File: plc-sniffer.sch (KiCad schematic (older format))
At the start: 3 parts, among them J101 TO EVSE, J102 DEBUG, J103 TO EV

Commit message: Add files via upload
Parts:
- J101, J102, J103: footprint (none) -> Connector_PinHeader_2.54mm:PinHeader_1x03_P2.54mm_Vertical
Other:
- note added: "0,1"
- note added: "2020/06/19"
- note added: "PLC Sniffer"
- note added: "Top layer schematic for\nPLC man-in-the-middle sniffer\nwith 15118 charging interface"
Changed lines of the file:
@@
 F 0 "J101" H 2418 3125 50  0000 C CNN
 F 1 "TO EVSE" H 2418 3216 50  0000 C CNN
-F 2 "" H 2500 3450 50  0001 C CNN
+F 2 "Connector_PinHeader_2.54mm:PinHeader_1x03_P2.54mm_Vertical" H 2500 3450 50  0001 C CNN
 F 3 "~" H 2500 3450 50  0001 C CNN
 	1    2500 3450
@@
 F 0 "J103" H 8830 3542 50  0000 L CNN
 F 1 "TO EV" H 8830 3451 50  0000 L CNN
-F 2 "" H 8750 3500 50  0001 C CNN
+F 2 "Connector_PinHeader_2.54mm:PinHeader_1x03_P2.54mm_Vertical" H 8750 3500 50  0001 C CNN
 F 3 "~" H 8750 3500 50  0001 C CNN
 	1    8750 3500
@@
 F 0 "J102" H 6980 2842 50  0000 L CNN
 F 1 "DEBUG" H 6980 2751 50  0000 L CNN
-F 2 "" H 6900 2800 50  0001 C CNN
+F 2 "Connector_PinHeader_2.54mm:PinHeader_1x03_P2.54mm_Vertical" H 6900 2800 50  0001 C CNN
 F 3 "~" H 6900 2800 50  0001 C CNN
 	1    6900 2800
@@
 Wire Wire Line
 	6450 5150 6900 5150
+Text Notes 7350 7500 0    50   ~ 0
+PLC Sniffer
+Text Notes 10600 7650 0    50   ~ 0
+0,1
+Text Notes 8100 7650 0    50   ~ 0
+2020/06/19
+Text Notes 7050 7050 0    100  ~ 0
+Top layer schematic for\nPLC man-in-the-middle sniffer\nwith 15118 charging interface
 $EndSCHEMATC

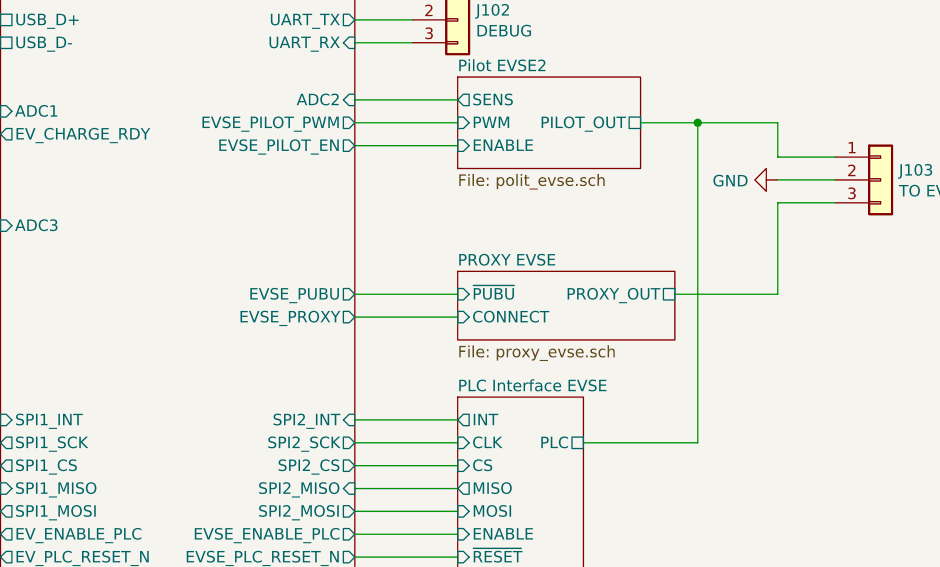
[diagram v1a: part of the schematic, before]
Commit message: Submited for production & smt assembly
v0.01
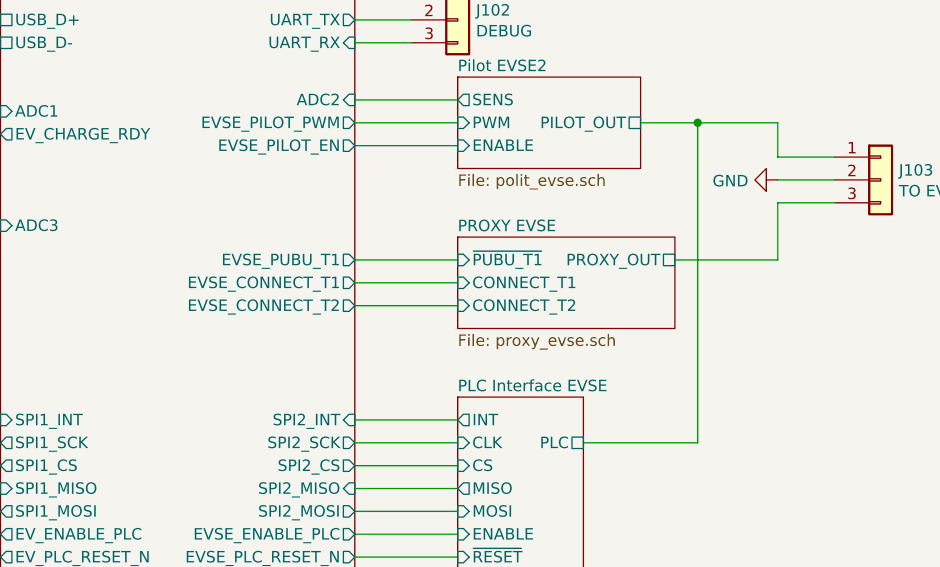
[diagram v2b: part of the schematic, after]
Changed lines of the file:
@@
-$EndSheet
-$Sheet
-S 6900 3900 950  300
-U 5EF016C6
-F0 "PROXY EVSE" 50
-F1 "proxy_evse.sch" 50
-F2 "PROXY_OUT" U R 7850 4000 50
-F3 "CONNECT" I L 6900 4100 50
-F4 "~PUBU" I L 6900 4000 50
 $EndSheet
 $Sheet
@@
 F5 "USB_D+" U L 4900 2800 50
 F6 "EVSE_PILOT_PWM" O R 6450 3250 50
-F7 "EVSE_PROXY" O R 6450 4100 50
-F8 "EVSE_PUBU" O R 6450 4000 50
-F9 "ADC1" I L 4900 3200 50
-F10 "ETH_CLK" I L 4900 6450 50
-F11 "ETH_MDIO" U L 4900 6250 50
-F12 "SPI1_SCK" O L 4900 4650 50
-F13 "SPI1_MISO" I L 4900 4850 50
-F14 "ETH_CRS_DV" I L 4900 5550 50
-F15 "SPI1_MOSI" O L 4900 4950 50
-F16 "ETH_TX_EN" O L 4900 5850 50
-F17 "ETH_TXD0" O L 4900 6050 50
-F18 "ETH_TXD1" O L 4900 5950 50
-F19 "ETH_MDC" O L 4900 6150 50
-F20 "ETH_RXD0" I L 4900 5750 50
-F21 "ETH_RXD1" I L 4900 5650 50
-F22 "MCO_2" O L 4900 6350 50
-F23 "SPI1_CS" O L 4900 4750 50
-F24 "SPI2_SCK" O R 6450 4650 50
-F25 "SPI2_MISO" I R 6450 4850 50
-F26 "SPI2_MOSI" O R 6450 4950 50
-F27 "SPI2_CS" O R 6450 4750 50
-F28 "EV_CHARGE_RDY" O L 4900 3300 50
-F29 "SPI2_INT" I R 6450 4550 50
-F30 "SPI1_INT" I L 4900 4550 50
-F31 "EV_ENABLE_PLC" O L 4900 5050 50
-F32 "EVSE_ENABLE_PLC" O R 6450 5050 50
-F33 "EVSE_PILOT_EN" O R 6450 3350 50
-F34 "~PHY_RESET" O L 4900 6750 50
-F35 "PHY_PDOWN" O L 4900 6850 50
-F36 "ADC3" I L 4900 3700 50
-F37 "UART_TX" O R 6450 2800 50
-F38 "EVSE_PLC_RESET_N" O R 6450 5150 50
-F39 "EV_PLC_RESET_N" O L 4900 5150 50
+F7 "ADC1" I L 4900 3200 50
+F8 "ETH_CLK" I L 4900 6450 50
+F9 "ETH_MDIO" U L 4900 6250 50
+F10 "SPI1_SCK" O L 4900 4650 50
+F11 "SPI1_MISO" I L 4900 4850 50
+F12 "ETH_CRS_DV" I L 4900 5550 50
+F13 "SPI1_MOSI" O L 4900 4950 50
+F14 "ETH_TX_EN" O L 4900 5850 50
+F15 "ETH_TXD0" O L 4900 6050 50
+F16 "ETH_TXD1" O L 4900 5950 50
+F17 "ETH_MDC" O L 4900 6150 50
+F18 "ETH_RXD0" I L 4900 5750 50
+F19 "ETH_RXD1" I L 4900 5650 50
+F20 "MCO_2" O L 4900 6350 50
+F21 "SPI1_CS" O L 4900 4750 50
+F22 "SPI2_SCK" O R 6450 4650 50
+F23 "SPI2_MISO" I R 6450 4850 50
+F24 "SPI2_MOSI" O R 6450 4950 50
+F25 "SPI2_CS" O R 6450 4750 50
+F26 "EV_CHARGE_RDY" O L 4900 3300 50
+F27 "SPI2_INT" I R 6450 4550 50
+F28 "SPI1_INT" I L 4900 4550 50
+F29 "EV_ENABLE_PLC" O L 4900 5050 50
+F30 "EVSE_ENABLE_PLC" O R 6450 5050 50
+F31 "EVSE_PILOT_EN" O R 6450 3350 50
+F32 "~PHY_RESET" O L 4900 6750 50
+F33 "PHY_PDOWN" O L 4900 6850 50
+F34 "ADC3" I L 4900 3700 50
+F35 "UART_TX" O R 6450 2800 50
+F36 "EVSE_PLC_RESET_N" O R 6450 5150 50
+F37 "EV_PLC_RESET_N" O L 4900 5150 50
+F38 "EVSE_CONNECT_T1" O R 6450 3950 50
+F39 "EVSE_PUBU_T1" O R 6450 3850 50
+F40 "EVSE_CONNECT_T2" O R 6450 4050 50
 $EndSheet
 Wire Wire Line
@@
 	7700 3250 7950 3250
 Wire Wire Line
-	6450 4000 6900 4000
-Wire Wire Line
-	6450 4100 6900 4100
-Wire Wire Line
 	6450 4550 6900 4550
 Wire Wire Line
@@
 	7950 4650 7950 3250
 Connection ~ 7950 3250
-Wire Wire Line
-	7850 4000 8300 4000
 Wire Wire Line
 	7950 3250 8300 3250
@@
 Wire Wire Line
 	8550 3600 8300 3600
-Wire Wire Line
-	8300 3600 8300 4000
 Wire Wire Line
 	8550 3500 8300 3500
@@
 Text Notes 7050 7050 0    100  ~ 0
 Top layer schematic for\nPLC man-in-the-middle sniffer\nwith 15118 charging interface
+$Sheet
+S 6900 3750 950  400
+U 5EF016C6
+F0 "PROXY EVSE" 50
+F1 "proxy_evse.sch" 50
+F2 "PROXY_OUT" U R 7850 3850 50
+F3 "~PUBU_T1" I L 6900 3850 50
+F4 "CONNECT_T1" I L 6900 3950 50
+F5 "CONNECT_T2" I L 6900 4050 50
+$EndSheet
+Wire Wire Line
+	6450 3850 6900 3850
+Wire Wire Line
+	6450 3950 6900 3950
+Wire Wire Line
+	6450 4050 6900 4050
+Wire Wire Line
+	7850 3850 8300 3850
+Wire Wire Line
+	8300 3850 8300 3600
 $EndSCHEMATC
